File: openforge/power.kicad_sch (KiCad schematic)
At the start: 44 parts, among them P1 conn_power_in, U2 TPS65217ARSLR, U4 TL5209DR

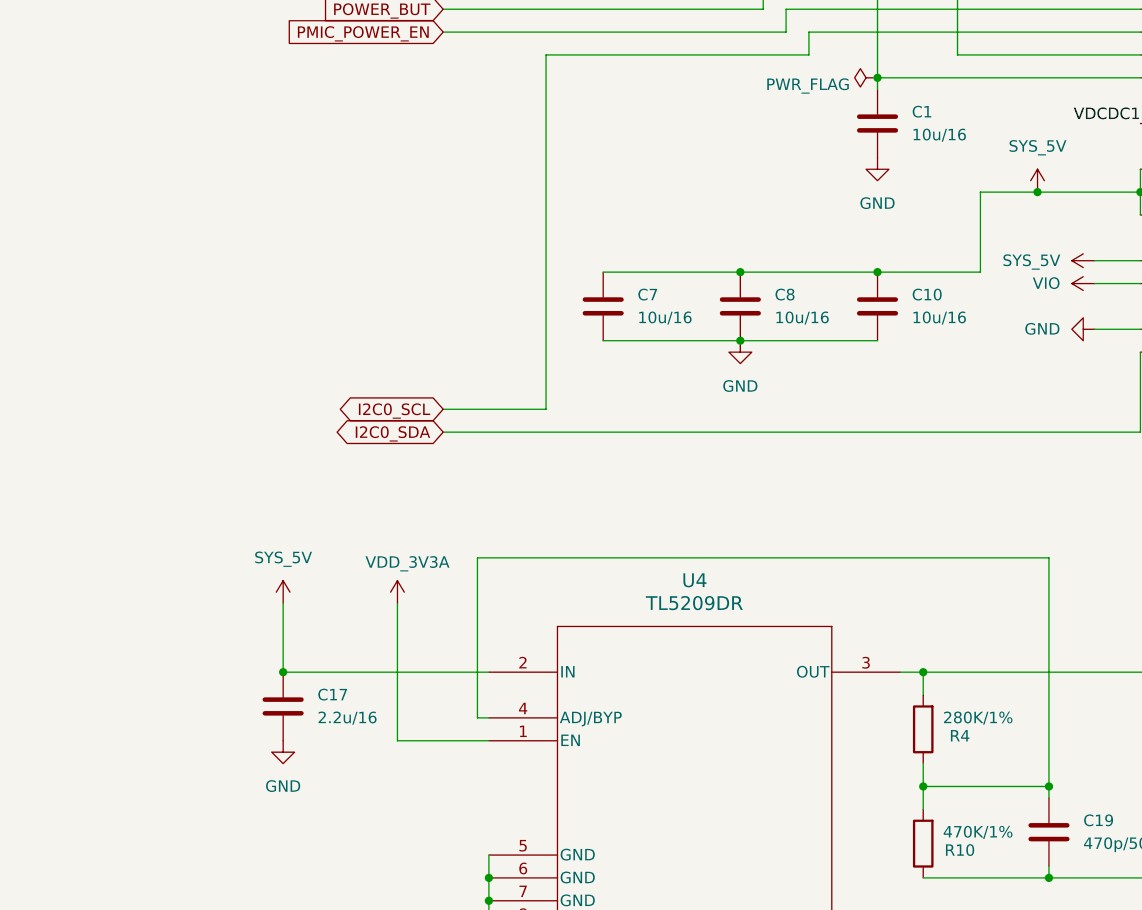
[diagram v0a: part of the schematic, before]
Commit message: added footprint associations
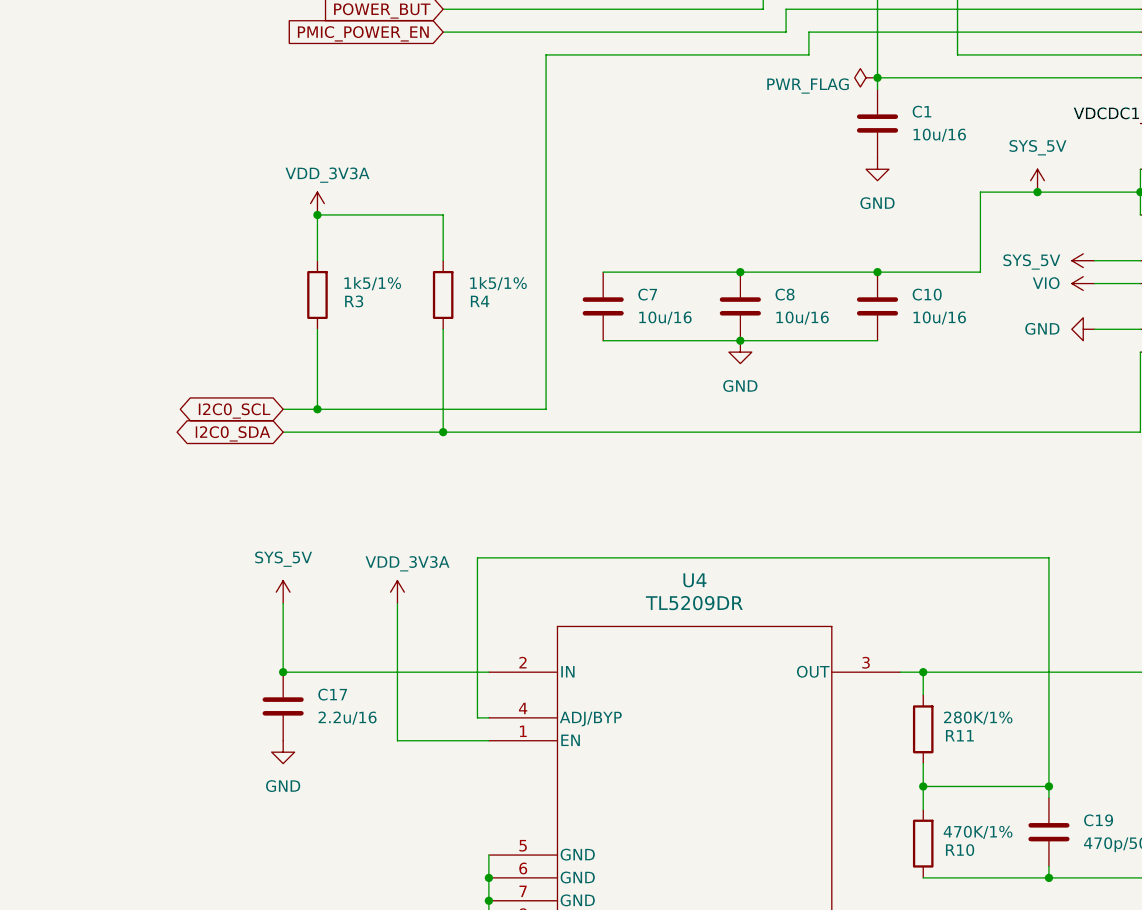
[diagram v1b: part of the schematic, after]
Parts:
- added R3, R4: 1k5/1%, Resistor_SMD:R_0402_1005Metric, symbol MT41K256M16TW-107_P:R
- R1, R10, R12, R5, R6, R7, R8, R9: footprint (none) -> Resistor_SMD:R_0402_1005Metric
- R11: renamed from R4; footprint (none) -> Resistor_SMD:R_0402_1005Metric
- S3: footprint (none) -> footprints:KMR2xxG_CNK
- TP1, TP5, TP6, TP7, TP8: footprint (none) -> TestPoint:TestPoint_Pad_1.5x1.5mm
- U2: footprint (none) -> footprints:RSL48_4P05X4P05
- U4: footprint (none) -> footprints:D8
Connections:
- net I2C0_SCL: now also R3.1
- net I2C0_SDA: now also R4.1
- net VDD_3V3A: now also R3.2, R4.2

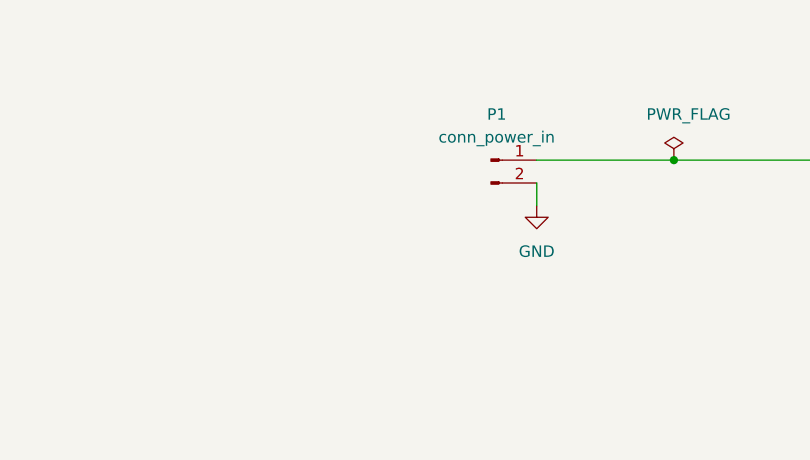
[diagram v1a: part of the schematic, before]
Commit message: Completed footprint association. Partially placed top side components on PCB
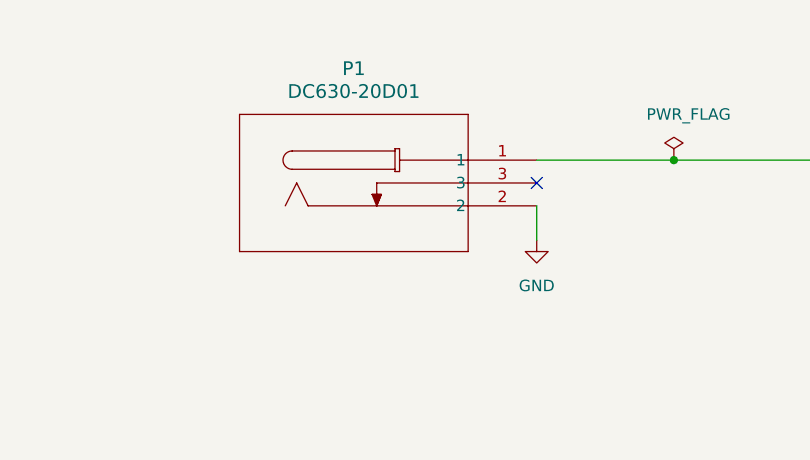
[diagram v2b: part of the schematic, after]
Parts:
- removed P1: conn_power_in, footprints:PJ-102A_CUD, symbol MT41K256M16TW-107_P:Conn_01x02_Pin
- added P1: DC630-20D01, footprints:PJ-102A_CUD, symbol 2024-06-09_17-22-08:PJ-102A
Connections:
- net GND: now also P1.2
- net VDD_5V: now also P1.1
- no-connect marks 9 -> 10
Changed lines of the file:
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@@
 	)
 	(no_connect
+		(at 100.33 77.47)
+	)
+	(no_connect
 		(at 251.46 100.33)
 	)
@@
 	(wire
 		(pts
+			(xy 100.33 80.01) (xy 100.33 83.82)
+		)
+		(stroke
+			(width 0)
+			(type default)
+		)
+	)
+	(wire
+		(pts
 			(xy 330.2 80.01) (xy 274.32 80.01)
 		)
@@
 	(wire
 		(pts
-			(xy 100.33 77.47) (xy 100.33 80.01)
-		)
-		(stroke
-			(width 0)
-			(type default)
-		)
-	)
-	(wire
-		(pts
 			(xy 151.13 120.65) (xy 151.13 123.19)
 		)
@@
 	)
 	(symbol
-		(lib_id "MT41K256M16TW-107_P:Conn_01x02_Pin")
-		(at 95.25 74.93 0)
-		(unit 1)
-		(exclude_from_sim no)
-		(in_bom yes)
-		(on_board yes)
-		(dnp no)
-		(fields_autoplaced yes)
-		(property "Reference" "P1"
-			(at 95.885 69.85 0)
-			(effects
-				(font
-					(size 1.27 1.27)
-				)
-			)
-		)
-		(property "Value" "conn_power_in"
-			(at 95.885 72.39 0)
-			(effects
-				(font
-					(size 1.27 1.27)
-				)
-			)
-		)
-		(property "Footprint" "footprints:PJ-102A_CUD"
-			(at 95.25 74.93 0)
-			(effects
-				(font
-					(size 1.27 1.27)
-				)
-				(hide yes)
-			)
-		)
-		(property "Datasheet" "~"
-			(at 95.25 74.93 0)
-			(effects
-				(font
-					(size 1.27 1.27)
-				)
-				(hide yes)
-			)
-		)
-		(property "Description" "Generic connector, single row, 01x02, script generated"
-			(at 95.25 74.93 0)
-			(effects
-				(font
-					(size 1.27 1.27)
-				)
-				(hide yes)
-			)
-		)
-		(pin "1"
-		)
-		(pin "2"
-		)
-		(instances
-			(project "openforge"
-				(path "/1648246a-cfdb-455c-9060-87fd156f3ecc/fee1a3f0-1fb6-4dc3-9a19-10db5903192c"
-					(reference "P1")
-					(unit 1)
-				)
-			)
-		)
-	)
-	(symbol
 		(lib_id "power:GND")
 		(at 118.11 224.79 0)
@@
 	(symbol
 		(lib_id "power:GND")
-		(at 100.33 80.01 0)
+		(at 100.33 83.82 0)
 		(unit 1)
 		(exclude_from_sim no)
@@
 		(fields_autoplaced yes)
 		(property "Reference" "#PWR05"
-			(at 100.33 86.36 0)
+			(at 100.33 90.17 0)
 			(effects
 				(font
@@
 		)
 		(property "Value" "GND"
-			(at 100.33 85.09 0)
+			(at 100.33 88.9 0)
 			(effects
 				(font
@@
 		)
 		(property "Footprint" ""
-			(at 100.33 80.01 0)
+			(at 100.33 83.82 0)
 			(effects
 				(font
@@
 		)
 		(property "Datasheet" ""
-			(at 100.33 80.01 0)
+			(at 100.33 83.82 0)
 			(effects
 				(font
@@
 		)
 		(property "Description" "Power symbol creates a global label with name \"GND\" , ground"
-			(at 100.33 80.01 0)
+			(at 100.33 83.82 0)
 			(effects
 				(font
@@
 					(unit 1)
 				)
+			)
+		)
+	)
+	(symbol
+		(lib_id "2024-06-09_17-22-08:PJ-102A")
+		(at 100.33 74.93 0)
+		(unit 1)
+		(exclude_from_sim no)
+		(in_bom yes)
+		(on_board yes)
+		(dnp no)
+		(fields_autoplaced yes)
+		(property "Reference" "P1"
+			(at 80.01 64.77 0)
+			(effects
+				(font
+					(size 1.524 1.524)
+				)
+			)
+		)
+		(property "Value" "DC630-20D01"
+			(at 80.01 67.31 0)
+			(effects
+				(font
+					(size 1.524 1.524)
+				)
+			)
+		)
+		(property "Footprint" "footprints:PJ-102A_CUD"
+			(at 100.33 74.93 0)
+			(effects
+				(font
+					(size 1.27 1.27)
+					(italic yes)
+				)
+				(hide yes)
+			)
+		)
+		(property "Datasheet" "PJ-102A"
+			(at 100.33 74.93 0)
+			(effects
+				(font
+					(size 1.27 1.27)
+					(italic yes)
+				)
+				(hide yes)
+			)
+		)
+		(property "Description" ""
+			(at 100.33 74.93 0)
+			(effects
+				(font
+					(size 1.27 1.27)
+				)
+				(hide yes)
+			)
+		)
+		(pin "1"
+		)
+		(pin "2"
+		)
+		(pin "3"
+		)
+		(instances
+			(project ""
+				(path "/1648246a-cfdb-455c-9060-87fd156f3ecc/fee1a3f0-1fb6-4dc3-9a19-10db5903192c"
+					(reference "P1")
+					(unit 1)
+				)

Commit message: fixed various footprints
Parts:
- TP1, TP5, TP6, TP7, TP8: footprint TestPoint:TestPoint_Pad_1.5x1.5mm -> TestPoint:TestPoint_Pad_D1.0mm
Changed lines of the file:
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@@
 			)
 		)
-		(property "Footprint" "TestPoint:TestPoint_Pad_1.5x1.5mm"
+		(property "Footprint" "TestPoint:TestPoint_Pad_D1.0mm"
 			(at 386.08 67.31 0)
 			(effects
@@
 			)
 		)
-		(property "Footprint" "TestPoint:TestPoint_Pad_1.5x1.5mm"
+		(property "Footprint" "TestPoint:TestPoint_Pad_D1.0mm"
 			(at 181.61 74.93 0)
 			(effects
@@
 			)
 		)
-		(property "Footprint" "TestPoint:TestPoint_Pad_1.5x1.5mm"
+		(property "Footprint" "TestPoint:TestPoint_Pad_D1.0mm"
 			(at 175.26 116.84 0)
 			(effects
@@
 			)
 		)
-		(property "Footprint" "TestPoint:TestPoint_Pad_1.5x1.5mm"
+		(property "Footprint" "TestPoint:TestPoint_Pad_D1.0mm"
 			(at 256.54 152.4 0)
 			(effects
@@
 			)
 		)
-		(property "Footprint" "TestPoint:TestPoint_Pad_1.5x1.5mm"
+		(property "Footprint" "TestPoint:TestPoint_Pad_D1.0mm"
 			(at 246.38 138.43 0)
 			(effects

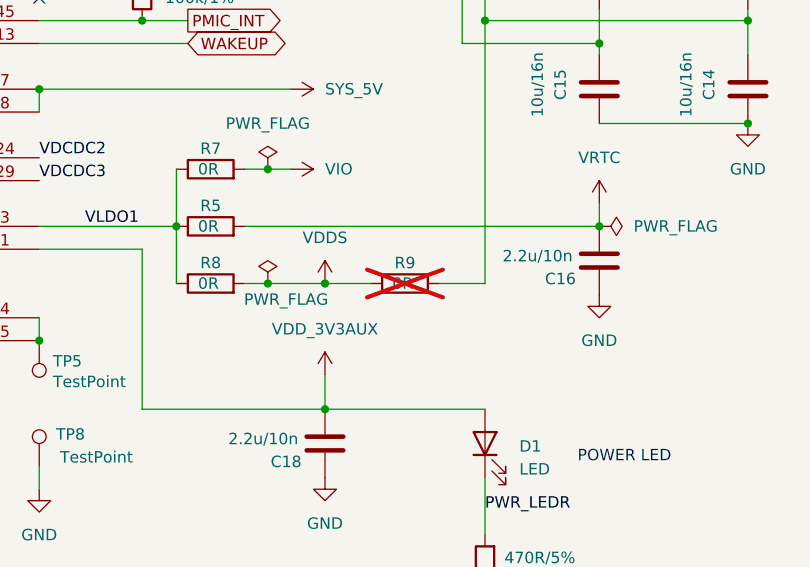
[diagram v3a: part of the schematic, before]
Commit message: fixed all errors and major warnings
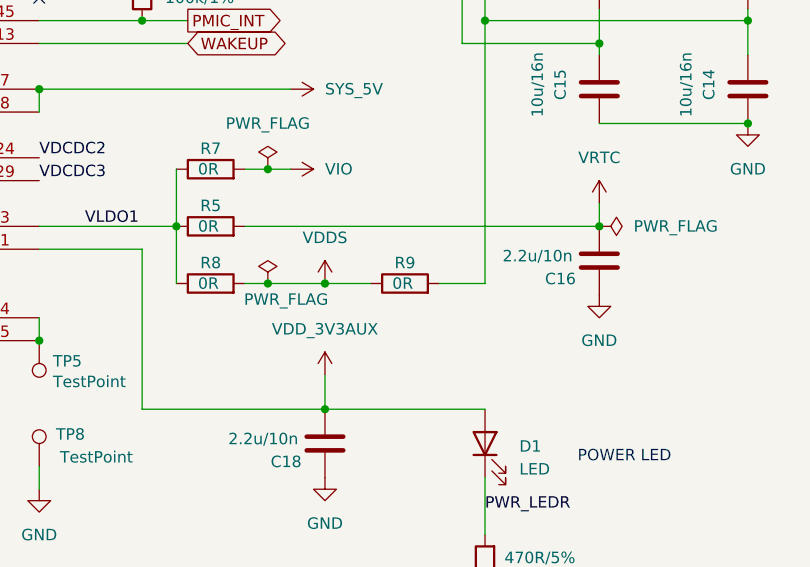
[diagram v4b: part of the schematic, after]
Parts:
- C1, C10, C11, C12, C13, C14, C15, C2, C4, C7, C8, C9: footprint Capacitor_SMD:C_0805_2012Metric -> footprints:C_0805_2012Metric
- C16, C17, C18, C19, C20, C3: footprint Capacitor_SMD:C_0402_1005Metric -> footprints:C_0402_1005Metric
- R1, R10, R11, R12, R3, R4, R5, R6, R7, R8: footprint Resistor_SMD:R_0402_1005Metric -> footprints:R_0402_1005Metric
- R9: footprint Resistor_SMD:R_0402_1005Metric -> footprints:R_0402_1005Metric; now fitted
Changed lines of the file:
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@@
 			)
 		)
-		(property "Footprint" "Capacitor_SMD:C_0402_1005Metric"
+		(property "Footprint" "footprints:C_0402_1005Metric"
 			(at 195.2752 209.55 0)
 			(effects
@@
 			)
 		)
-		(property "Footprint" "Capacitor_SMD:C_0805_2012Metric"
+		(property "Footprint" "footprints:C_0805_2012Metric"
 			(at 140.6652 82.55 0)
 			(effects
@@
 			)
 		)
-		(property "Footprint" "Resistor_SMD:R_0402_1005Metric"
+		(property "Footprint" "footprints:R_0402_1005Metric"
 			(at 168.148 200.66 90)
 			(effects
@@
 		(in_bom yes)
 		(on_board yes)
-		(dnp yes)
+		(dnp no)
 		(property "Reference" "R9"
 			(at 292.1 129.794 90)
@@
 			)
 		)
-		(property "Footprint" "Resistor_SMD:R_0402_1005Metric"
+		(property "Footprint" "footprints:R_0402_1005Metric"
 			(at 292.1 133.858 90)
 			(effects
@@
 			)
 		)
-		(property "Footprint" "Capacitor_SMD:C_0805_2012Metric"
+		(property "Footprint" "footprints:C_0805_2012Metric"
 			(at 312.7248 85.09 0)
 			(effects
@@
 			)
 		)
-		(property "Footprint" "Capacitor_SMD:C_0402_1005Metric"
+		(property "Footprint" "footprints:C_0402_1005Metric"
 			(at 282.2448 146.05 0)
 			(effects
@@
 			)
 		)
-		(property "Footprint" "Resistor_SMD:R_0402_1005Metric"
+		(property "Footprint" "footprints:R_0402_1005Metric"
 			(at 270.51 127.508 90)
 			(effects
@@
 			)
 		)
-		(property "Footprint" "Resistor_SMD:R_0402_1005Metric"
+		(property "Footprint" "footprints:R_0402_1005Metric"
 			(at 114.808 152.4 90)
 			(effects
@@
 			)
 		)
-		(property "Footprint" "Resistor_SMD:R_0402_1005Metric"
+		(property "Footprint" "footprints:R_0402_1005Metric"
 			(at 304.8 77.978 90)
 			(effects
@@
 			)
 		)
-		(property "Footprint" "Resistor_SMD:R_0402_1005Metric"
+		(property "Footprint" "footprints:R_0402_1005Metric"
 			(at 168.148 213.36 90)
 			(effects
@@
 			)
 		)
-		(property "Footprint" "Capacitor_SMD:C_0402_1005Metric"
+		(property "Footprint" "footprints:C_0402_1005Metric"
 			(at 96.2152 201.93 0)
 			(effects
@@
 			)
 		)
-		(property "Footprint" "Resistor_SMD:R_0402_1005Metric"
+		(property "Footprint" "footprints:R_0402_1005Metric"
 			(at 264.668 99.06 90)
 			(effects
@@
 			)
 		)
-		(property "Footprint" "Capacitor_SMD:C_0805_2012Metric"
+		(property "Footprint" "footprints:C_0805_2012Metric"
 			(at 274.32 66.3448 0)
 			(effects
@@
 			)
 		)
-		(property "Footprint" "Capacitor_SMD:C_0805_2012Metric"
+		(property "Footprint" "footprints:C_0805_2012Metric"
 			(at 345.7448 85.09 0)
 			(effects
@@
 			)
 		)
-		(property "Footprint" "Capacitor_SMD:C_0805_2012Metric"
+		(property "Footprint" "footprints:C_0805_2012Metric"
 			(at 162.2552 157.48 0)
 			(effects
@@
 			)
 		)
-		(property "Footprint" "Resistor_SMD:R_0402_1005Metric"
+		(property "Footprint" "footprints:R_0402_1005Metric"
 			(at 270.51 121.158 90)
 			(effects
@@
 			)
 		)
-		(property "Footprint" "Capacitor_SMD:C_0805_2012Metric"
+		(property "Footprint" "footprints:C_0805_2012Metric"
 			(at 147.0152 157.48 0)
 			(effects
@@
 			)
 		)
-		(property "Footprint" "Capacitor_SMD:C_0805_2012Metric"
+		(property "Footprint" "footprints:C_0805_2012Metric"
 			(at 162.2552 137.16 0)
 			(effects
@@
 			)
 		)
-		(property "Footprint" "Resistor_SMD:R_0402_1005Metric"
+		(property "Footprint" "footprints:R_0402_1005Metric"
 			(at 270.51 133.858 90)
 			(effects
@@
 			)
 		)
-		(property "Footprint" "Capacitor_SMD:C_0805_2012Metric"
+		(property "Footprint" "footprints:C_0805_2012Metric"
 			(at 312.7248 106.68 0)
 			(effects
@@
 			)
 		)
-		(property "Footprint" "Capacitor_SMD:C_0805_2012Metric"
+		(property "Footprint" "footprints:C_0805_2012Metric"
 			(at 170.18 99.3648 0)
 			(effects
@@
 			)
 		)
-		(property "Footprint" "Capacitor_SMD:C_0805_2012Metric"
+		(property "Footprint" "footprints:C_0805_2012Metric"
 			(at 329.2348 85.09 0)
 			(effects
@@
 			)
 		)
-		(property "Footprint" "Capacitor_SMD:C_0402_1005Metric"
+		(property "Footprint" "footprints:C_0402_1005Metric"
 			(at 312.7248 125.73 0)
 			(effects
@@
 			)
 		)
-		(property "Footprint" "Capacitor_SMD:C_0805_2012Metric"
+		(property "Footprint" "footprints:C_0805_2012Metric"
 			(at 131.7752 157.48 0)
 			(effects
@@
 			)
 		)
-		(property "Footprint" "Resistor_SMD:R_0402_1005Metric"
+		(property "Footprint" "footprints:R_0402_1005Metric"
 			(at 100.838 152.4 90)
 			(effects
@@
 			)
 		)
-		(property "Footprint" "Resistor_SMD:R_0402_1005Metric"
+		(property "Footprint" "footprints:R_0402_1005Metric"
 			(at 302.768 163.83 90)
 			(effects
@@
 			)
 		)
-		(property "Footprint" "Capacitor_SMD:C_0402_1005Metric"
+		(property "Footprint" "footprints:C_0402_1005Metric"
 			(at 181.3052 215.9 0)
 			(effects
@@
 			)
 		)
-		(property "Footprint" "Capacitor_SMD:C_0402_1005Metric"
+		(property "Footprint" "footprints:C_0402_1005Metric"
 			(at 162.56 88.5952 0)
 			(effects
@@
 			)
 		)
-		(property "Footprint" "Capacitor_SMD:C_0805_2012Metric"
+		(property "Footprint" "footprints:C_0805_2012Metric"
 			(at 329.2348 106.68 0)
 			(effects
